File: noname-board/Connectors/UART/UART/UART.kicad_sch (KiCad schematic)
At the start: 1 part, among them U1 SN74LV8153N

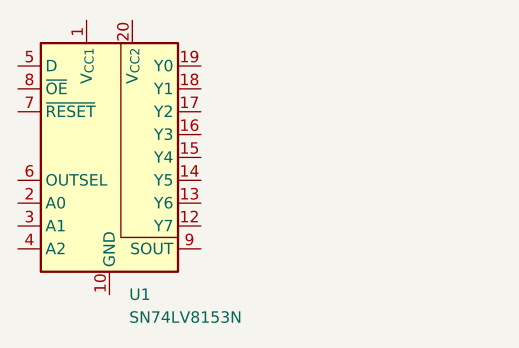
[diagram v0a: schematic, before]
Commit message: GPIO, USBC
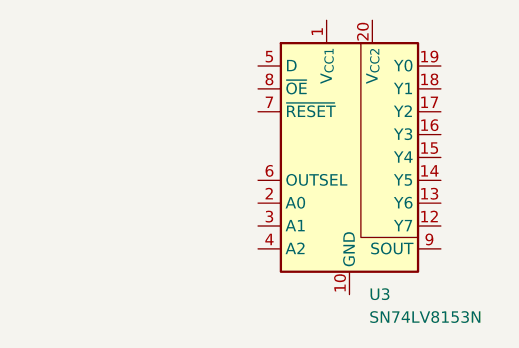
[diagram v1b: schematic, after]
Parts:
- removed U1: SN74LV8153N, Package_DIP:DIP-20_W7.62mm, symbol Interface:SN74LV8153N
- added U3: SN74LV8153N, Package_DIP:DIP-20_W7.62mm, symbol Interface:SN74LV8153N
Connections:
- new net: U3.10 (GND), U3.11 (GND)
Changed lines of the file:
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@@
 (kicad_sch (version 20230121) (generator eeschema)
   (paper "A4")
-  (symbol (lib_id "Interface:SN74LV8153N") (at 105.41 54.61 0) (unit 1)
+  (symbol (lib_id "Interface:SN74LV8153N") (at 132.08 54.61 0) (unit 1)
     (in_bom yes) (on_board yes) (dnp no) (fields_autoplaced)
-    (property "Reference" "U1" (at 107.6041 69.85 0)
+    (property "Reference" "U3" (at 134.2741 69.85 0)
       (effects (font (size 1.27 1.27)) (justify left))
     )
-    (property "Value" "SN74LV8153N" (at 107.6041 72.39 0)
+    (property "Value" "SN74LV8153N" (at 134.2741 72.39 0)
       (effects (font (size 1.27 1.27)) (justify left))
     )
-    (property "Footprint" "Package_DIP:DIP-20_W7.62mm" (at 105.41 54.61 0)
+    (property "Footprint" "Package_DIP:DIP-20_W7.62mm" (at 132.08 54.61 0)
       (effects (font (size 1.27 1.27)) hide)
     )
-    (property "Datasheet" "https://www.ti.com/lit/ds/symlink/sn74lv8153.pdf" (at 105.41 54.61 0)
+    (property "Datasheet" "https://www.ti.com/lit/ds/symlink/sn74lv8153.pdf" (at 132.08 54.61 0)
       (effects (font (size 1.27 1.27)) hide)
     )
@@
       (project "UART"
         (path "/2647965b-4766-434f-aba1-02b6b336399e"
-          (reference "U1") (unit 1)
+          (reference "U3") (unit 1)
         )
       )
